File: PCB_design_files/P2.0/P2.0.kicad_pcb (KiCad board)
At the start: 4 copper layers, 16 x 17 mm, 0 parts

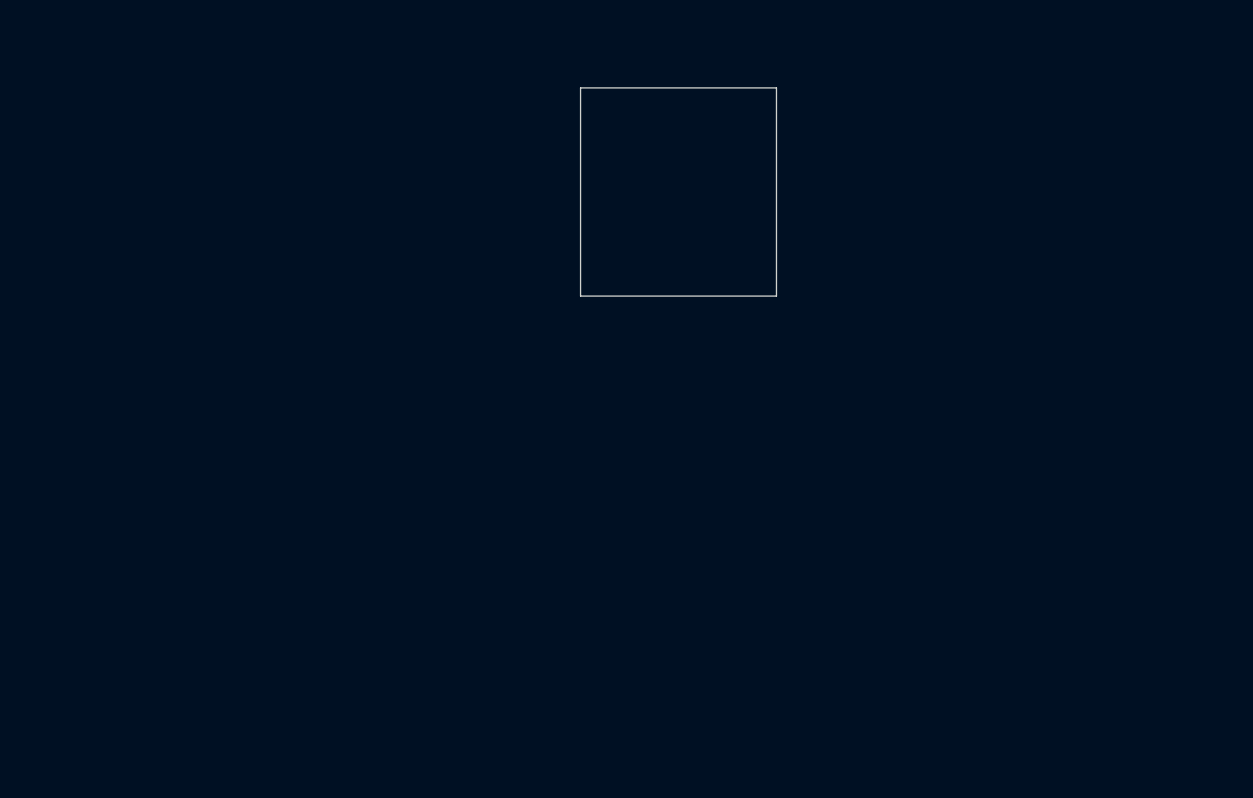
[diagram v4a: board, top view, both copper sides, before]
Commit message: Added decoupling capacitors and updated layout
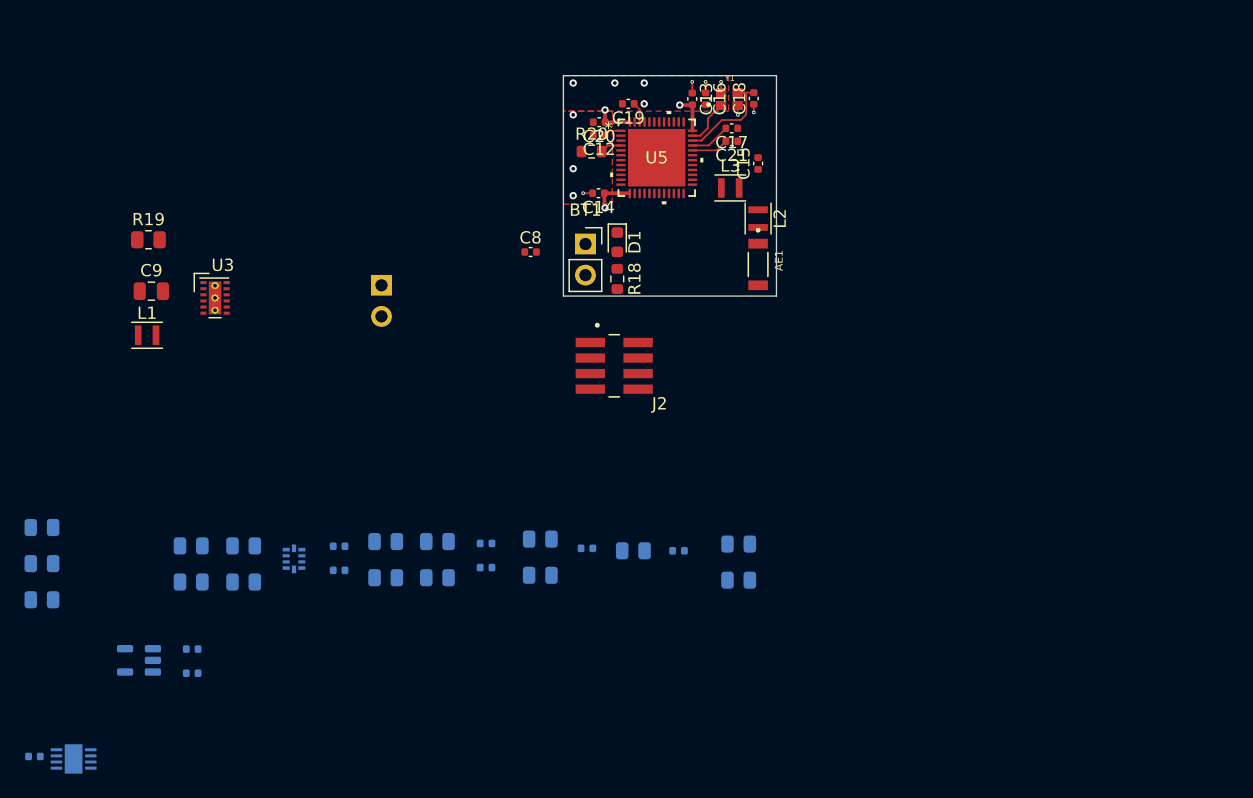
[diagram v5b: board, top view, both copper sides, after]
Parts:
- added AE1: Antenna_Chip, Library:XDCR_2450AT18B100E, F.Cu at (89.5, 46.4)
- added BT1: BHSD-1225-SM, Connector_PinSocket_2.54mm:PinSocket_1x02_P2.54mm_Vertical, F.Cu at (75.4, 44.8)
- added C1: 10uF, Capacitor_SMD:C_0402_1005Metric, B.Cu at (30.4, 86.6)
- added C10: 1uF, Capacitor_SMD:C_0402_1005Metric, B.Cu at (43.3, 77.8)
- added C11: 1uF, Capacitor_SMD:C_0402_1005Metric, B.Cu at (43.3, 79.8)
- added C12: 100nF, Capacitor_SMD:C_0402_1005Metric, F.Cu at (76.5, 35.8)
- added C13: 100nF, Capacitor_SMD:C_0402_1005Metric, F.Cu at (84.1, 32.9)
- added C14: 100nF, Capacitor_SMD:C_0402_1005Metric, F.Cu at (76.5, 40.6)
- added C15: 1.2pF, Capacitor_SMD:C_0402_1005Metric, F.Cu at (89.5, 38.2)
- added C16: 12pF, Capacitor_SMD:C_0402_1005Metric, F.Cu at (85.2, 32.9)
- added C17: 100pF, Capacitor_SMD:C_0402_1005Metric, F.Cu at (87.3, 35.3)
- added C18: 12pF, Capacitor_SMD:C_0402_1005Metric, F.Cu at (89.1, 32.9)
- added C19: 1uF, Capacitor_SMD:C_0402_1005Metric, F.Cu at (78.9, 33.3)
- added C2: 10uF, Capacitor_SMD:C_0402_1005Metric, B.Cu at (55.3, 69.4)
- added C20: 4.7uF, Capacitor_SMD:C_0402_1005Metric, F.Cu at (76.5, 34.8)
- added C21: ~, Capacitor_SMD:C_0402_1005Metric, F.Cu at (87.3, 36.4)
- added C3: 0.1uF, Capacitor_SMD:C_0402_1005Metric, B.Cu at (55.3, 71.4)
- added C4: 0.1uF, Capacitor_SMD:C_0402_1005Metric, B.Cu at (67.3, 69.2)
- added C5: 0.1uF, Capacitor_SMD:C_0402_1005Metric, B.Cu at (67.3, 71.2)
- added C6: 10nF, Capacitor_SMD:C_0402_1005Metric, B.Cu at (75.5, 69.6)
- added C7: 10uF, Capacitor_SMD:C_0402_1005Metric, B.Cu at (83.0, 69.8)
- added C8: 2.2uF, Capacitor_SMD:C_0402_1005Metric, F.Cu at (70.9, 45.4)
- added C9: 33uF, Capacitor_SMD:C_0805_2012Metric, F.Cu at (40.0, 48.6)
- added D1: LED, LED_SMD:LED_0603_1608Metric, F.Cu at (78.0, 44.6)
- added J1: EEG_IN, Connector_PinHeader_2.54mm:PinHeader_1x02_P2.54mm_Vertical, B.Cu at (58.7, 48.1)
- added J2: 20021121-00008C4LF, 20021121_00008C4LF:AMPHENOL_20021121-00008C4LF, F.Cu at (77.8, 54.7)
- added L1: 2.2uH, Inductor_SMD:L_Murata_DFE201610P, F.Cu at (39.6, 52.2)
- added L2: 3.3nH, Inductor_SMD:L_Murata_DFE201610P, F.Cu at (89.5, 42.7)
- added L3: 2.7nH, Inductor_SMD:L_Murata_DFE201610P, F.Cu at (87.2, 40.2)
- added R1: 68k, Resistor_SMD:R_0805_2012Metric, B.Cu at (31.0, 67.9)
- added R10: 604, Resistor_SMD:R_0805_2012Metric, B.Cu at (63.3, 69.0)
- added R11: 16k, Resistor_SMD:R_0805_2012Metric, B.Cu at (63.3, 72.0)
- added R12: 2.49k, Resistor_SMD:R_0805_2012Metric, B.Cu at (71.7, 68.8)
- added R13: 49.9k, Resistor_SMD:R_0805_2012Metric, B.Cu at (71.7, 71.8)
- added R14: 10k, Resistor_SMD:R_0805_2012Metric, B.Cu at (79.3, 69.8)
- added R16: 100k, Resistor_SMD:R_0805_2012Metric, B.Cu at (87.9, 69.2)
- added R17: 100k, Resistor_SMD:R_0805_2012Metric, B.Cu at (87.9, 72.2)
- added R18: 1.1k, Resistor_SMD:R_0603_1608Metric, F.Cu at (78.0, 47.6)
- added R19: 1.1k, Resistor_SMD:R_0805_2012Metric, F.Cu at (39.7, 44.4)
- added R2: 68k, Resistor_SMD:R_0805_2012Metric, B.Cu at (31.0, 70.8)
- added R20: 10k, Resistor_SMD:R_0603_1608Metric, F.Cu at (75.9, 37.2)
- added R3: 8.2k, Resistor_SMD:R_0805_2012Metric, B.Cu at (31.0, 73.8)
- added R4: 100k, Resistor_SMD:R_0805_2012Metric, B.Cu at (43.2, 69.4)
- added R5: 1k, Resistor_SMD:R_0805_2012Metric, B.Cu at (43.2, 72.3)
- added R6: 20k, Resistor_SMD:R_0805_2012Metric, B.Cu at (47.5, 69.4)
- added R7: 1k, Resistor_SMD:R_0805_2012Metric, B.Cu at (47.5, 72.3)
- added R8: 100k, Resistor_SMD:R_0805_2012Metric, B.Cu at (59.1, 69.0)
- added R9: 100k, Resistor_SMD:R_0805_2012Metric, B.Cu at (59.1, 72.0)
- added U1: INA819IDRGR, Package_SON:WSON-8-1EP_3x3mm_P0.5mm_EP1.45x2.4mm, B.Cu at (33.6, 86.8)
- added U2: TLV9102, Package_DFN_QFN:Texas_R-PUQFN-N10, B.Cu at (51.6, 70.5)
- added U3: TPS61094, Package_SON:WSON-12-1EP_3x2mm_P0.5mm_EP1x2.65_ThermalVias, F.Cu at (45.1, 49.1)
- added U4: TPS60400, Package_TO_SOT_SMD:SOT-23-5, B.Cu at (38.9, 78.8)
- added U5: NRF52832-QFAA-R, Library:QFN-48_NOR, F.Cu at (81.2, 37.7)
- added Y1: 32MHz, ECS_320_8_37CKM:XTAL_ECS-320-8-37CKM, F.Cu at (87.2, 32.9)
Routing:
- net +3V3: track 0.00 -> 9.52 mm, vias 0 -> 3
- net Net-(U5-XC1): track 0.00 -> 9.00 mm
- net GND: track 0.00 -> 4.92 mm, vias 0 -> 13
- net Net-(U5-XC2): track 0.00 -> 3.90 mm
- net Net-(U5-DEC3): track 0.00 -> 3.31 mm
- net Net-(U5-DEC2): track 0.00 -> 3.04 mm
- net Net-(U5-P0.02/AIN0): track 0.00 -> 1.78 mm
- net Net-(U5-DEC4): track 0.00 -> 1.66 mm
- net Net-(U5-DEC1): track 0.00 -> 1.44 mm
- added copper zone on F.Cu, net GND
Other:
- board size 16 x 17 mm -> 17.4 x 18 mm

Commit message: PCB layout updates
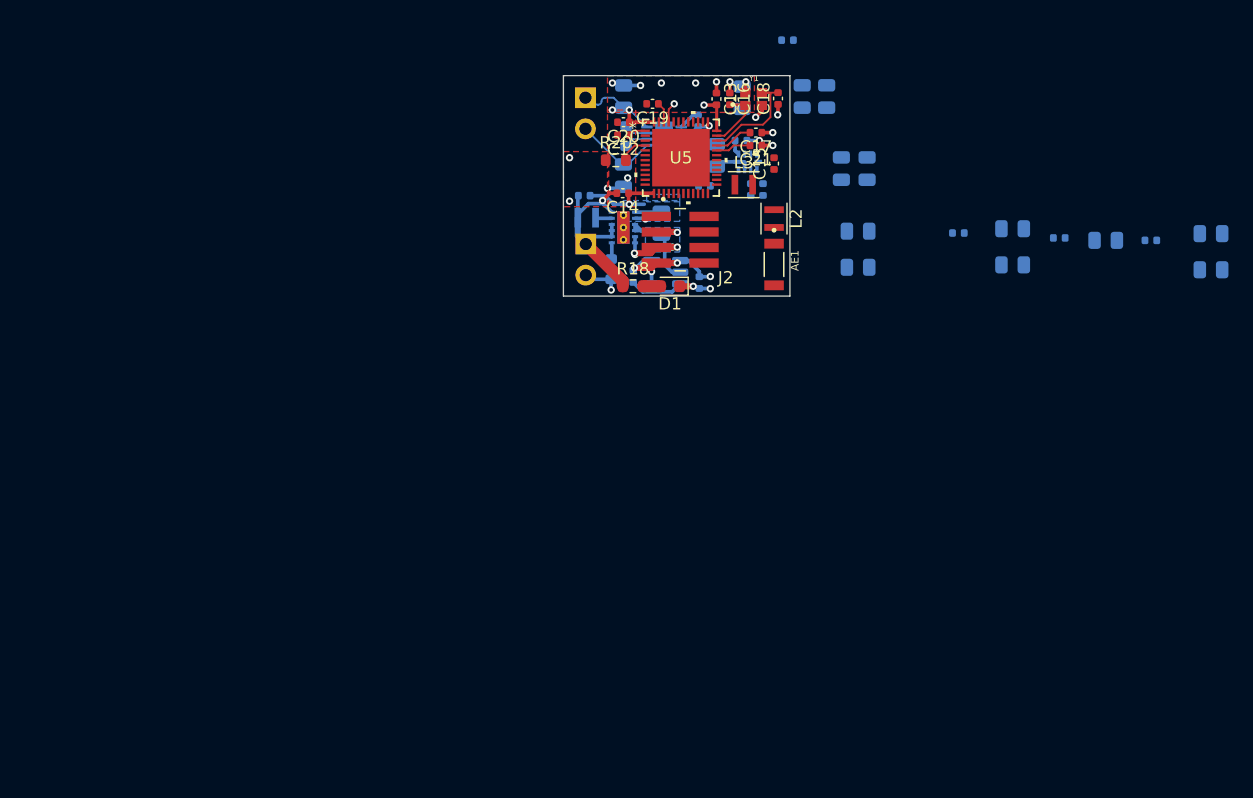
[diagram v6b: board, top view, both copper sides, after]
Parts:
- added C22: .1uF, Capacitor_SMD:C_0402_1005Metric, B.Cu at (82.7, 38.2)
- added C23: .1uF, Capacitor_SMD:C_0402_1005Metric, B.Cu at (84.6, 34.7)
- added C24: .1uF, Capacitor_SMD:C_0402_1005Metric, B.Cu at (88.9, 40.3)
- added C25: .1uF, Capacitor_SMD:C_0402_1005Metric, B.Cu at (88.1, 36.3)
- BT1, C8, C9, L1, U3: moved to B.Cu
- R19: footprint Resistor_SMD:R_0805_2012Metric -> Resistor_SMD:R_0603_1608Metric; moved to B.Cu
- R3: footprint Resistor_SMD:R_0805_2012Metric -> Resistor_SMD:R_0603_1608Metric
- moved C1 73.6 mm to (84.6, 36.8), turned to -90 degrees
- moved U1 70.1 mm to (81.8, 35.9), turned to 0 degrees
- moved R4 63.6 mm to (95.1, 32.7), turned to 90 degrees
- moved R2 60.9 mm to (78.5, 32.7), turned to 90 degrees
- moved R3 60.9 mm to (78.7, 35.9), turned to 90 degrees
- moved R6 59.5 mm to (98.4, 38.6), turned to 90 degrees
- moved R7 59.4 mm to (96.3, 38.6), turned to -90 degrees
- moved R1 55.5 mm to (78.5, 39.2), turned to -90 degrees
- moved R5 55.3 mm to (86.1, 37.5), turned to -90 degrees
- moved U4 53.5 mm to (82.0, 47.0)
- moved C11 52.3 mm to (84.7, 47.9), turned to 90 degrees
- moved C5 49.6 mm to (91.9, 28.1)
- moved U2 49.2 mm to (88.7, 38.0), turned to -90 degrees
- moved C10 47.2 mm to (79.3, 47.4), turned to -90 degrees
- moved R10 47.0 mm to (93.1, 32.7), turned to -90 degrees
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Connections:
- J2 pad 5: NRST -> SWO
- J2 pad 6: SWO -> NRST
- J2 pad 7: SWDCLK -> SWDIO
- J2 pad 8: SWDIO -> SWDCLK
- U3 pad 9: unconnected-(U3-VOUT-Pad9) -> +3V3
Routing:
- net GND: track 4.92 -> 38.6 mm, vias 13 -> 30
- net Net-(BT1-+): track 0.00 -> 16.0 mm
- net +3V3: track 9.52 -> 20.9 mm, vias 3 -> 6
- net /EEG+: track 0.00 -> 6.87 mm
- net /EEG-: track 0.00 -> 6.62 mm
- net -3V3: track 0.00 -> 6.27 mm, vias 0 -> 1
- net Net-(U4-CFLY-): track 0.00 -> 4.43 mm
- net Net-(U2-IN1+): track 0.00 -> 3.07 mm
- net Net-(U4-CFLY+): track 0.00 -> 1.96 mm
- net Net-(R3-Pad2): track 0.00 -> 1.94 mm
- net Net-(R3-Pad1): track 0.00 -> 1.94 mm
- net Net-(U1-OUT): track 0.00 -> 1.44 mm
- net Net-(D1-A): track 0.00 -> 1.41 mm
- net Net-(U3-OSEL): track 0.00 -> 1.35 mm
- net Net-(U3-SW): track 0.00 -> 1.35 mm
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- added copper zone on B.Cu, net +3V3
- added copper zone on B.Cu, net GND
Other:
- board size 17.4 x 18 mm -> 18.5 x 18 mm
